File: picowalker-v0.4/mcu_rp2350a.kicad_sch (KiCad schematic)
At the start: 0 parts

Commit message: v0.4: schematic laid out first draft
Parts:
- added C1, C3, C7: 4.7u, Capacitor_SMD:C_0402_1005Metric, symbol Device:C
- added C10, C11, C12, C13, C14, C5, C6, C8, C9: 0.1u, Capacitor_SMD:C_0402_1005Metric, symbol Device:C
- added C2, C4: 15p, Capacitor_SMD:C_0201_0603Metric, symbol Device:C
- added L1: 3.3u, symbol picowalker:L_Polarised
- added R1: 33R, Resistor_SMD:R_0402_1005Metric, symbol Device:R
- added R2, R3, R4: 1k, Resistor_SMD:R_0402_1005Metric, symbol Device:R
- added R5, R6: 22R, Resistor_SMD:R_0402_1005Metric, symbol Device:R
- added SW1: ~{BOOT}, symbol picowalker:SW_SPST_Shield
- added SW2: RUN, symbol picowalker:SW_SPST_Shield
- added TP1: MCU_1V1, TestPoint:TestPoint_Pad_1.0x1.0mm, symbol Connector:TestPoint
- added U1: RP2350A-QFN60, symbol picowalker:RP2350A-QFN60
- added Y1: ABM8-272-T3, symbol Device:Crystal_GND24
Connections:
- new net: C4.1, R4.1, Y1.3
- new net: R6.1, U1.51 (USB_DM)
- new net: R5.1, U1.52 (USB_DP)
- new net: R2.2, SW2.1 (A)
- new net +1.1V: C1.1, C5.1, C6.1, C7.1, L1.1, TP1.1, U1.23 (DVDD), U1.39 (DVDD), U1.50 (VREG_FB), U1.6 (DVDD)
- new net +3.3V: C10.1, C11.1, C12.1, C13.1, C14.1, C8.1, C9.1, R1.1, U1.1 (IOVDD), U1.11 (IOVDD), U1.20 (IOVDD), U1.30 (IOVDD), U1.38 (IOVDD), U1.44 (ADC_AVDD), U1.45 (IOVDD), U1.49 (VREG_VIN), U1.53 (USB_OTP_VDD), U1.54 (QSPI_IOVDD)
- new net ACCEL_INT: U1.35 (GPIO23)
- new net DN: R6.2
- new net DP: R5.2
- new net GND: C1.2, C10.2, C11.2, C12.2, C13.2, C14.2, C2.2, C3.2, C4.2, C5.2, C6.2, C7.2, C8.2, C9.2, R2.1, SW1.1 (A), SW1.3 (SHIELD), SW2.3 (SHIELD), U1.47 (VREG_PGND), U1.61 (GND), Y1.2, Y1.4
- new net IRDA_SD: U1.19 (GPIO15)
- new net L: U1.28 (GPIO17)
- new net M: U1.27 (GPIO16)
- new net MISO: U1.32 (GPIO20)
- new net MOSI: U1.31 (GPIO19)
- new net PWR_EN: U1.9 (GPIO6)
- new net R: U1.40 (GPIO26_ADC0)
- new net RTC_CLK: U1.34 (GPIO22)
- new net RUN: SW2.2 (B), U1.26 (RUN)
- new net RX: U1.18 (GPIO14), U1.43 (GPIO29_ADC3)
- new net SCK: U1.12 (GPIO8), U1.29 (GPIO18), U1.56 (QSPI_SCLK)
- new net SCL: U1.3 (GPIO1)
- new net SD0: U1.16 (GPIO12), U1.57 (QSPI_SD0)
- new net SD1: U1.15 (GPIO11), U1.59 (QSPI_SD1)
- new net SD2: U1.14 (GPIO10), U1.58 (QSPI_SD2)
- new net SD3: U1.13 (GPIO9), U1.55 (QSPI_SD3)
- new net SDA: U1.2 (GPIO0)
- new net SOUND_PWM: U1.4 (GPIO2)
- new net SWCLK: U1.24 (SWCLK)
- new net SWDIO: U1.25 (SWDIO)
- new net TX: U1.17 (GPIO13), U1.42 (GPIO28_ADC2)
- new net VREG_AVDD: C3.1, R1.2, U1.46 (VREG_AVDD)
- new net VREG_LX: L1.2, U1.48 (VREG_LX)
- new net XIN: C2.1, U1.21 (XIN), Y1.1
- new net XOUT: R4.2, U1.22 (XOUT)
- new net ~{ACCEL_CS}: U1.33 (GPIO21)
- new net ~{BAT_INT}: U1.5 (GPIO3)
- new net ~{BOOT}: R3.1, SW1.2 (B)
- new net ~{CE}: U1.7 (GPIO4)
- new net ~{EEPROM_CS}: U1.36 (GPIO24)
- new net ~{FLASH_CS}: R3.2, U1.60 (QSPI_SS)
- new net ~{RST}: U1.10 (GPIO7)
- new net ~{SCREEN_CS}: U1.8 (GPIO5)
- no-connect marks 0 -> 2
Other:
- note added: "Ensure ground plane is >1.0 mm from surface"
- note added: "I2C0"
- note added: "PIO"
- note added: "SPI0"
- note added: "TODO: NEEDS CHECKING"

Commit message: v0.4: more rationalisation
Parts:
- added C37: 4.7u, Capacitor_SMD:C_0402_1005Metric, symbol Device:C
- R1: value 33R -> 47R
- TP1: now left out of the parts list
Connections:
- net +3.3V: now also C37.1
- net GND: now also C37.2
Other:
- note added: ""33R and 4.7u is adequate" -3 dB cutoff (1/2piRC) for 33R is 1026 Hz. 47R is 720 Hz."
- note removed: "TODO: NEEDS CHECKING"
- moved on the sheet: C1, C3, L1, R1, TP1

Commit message: v0.4: first rough placement of PCB
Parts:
- C1, C37: footprint Capacitor_SMD:C_0402_1005Metric -> picowalker:C_0402_1005Metric_Smaller
- L1: footprint (none) -> picowalker:L_0805_2016Metric
- SW1, SW2: footprint (none) -> picowalker:435151014824
- U1: footprint (none) -> Package_DFN_QFN:QFN-60-1EP_7x7mm_P0.4mm_EP3.4x3.4mm_ThermalVias
- Y1: footprint (none) -> picowalker:ABM8272T3
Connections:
- net DN renamed USB.DN
- net DP renamed USB.DP
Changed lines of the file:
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@@
 		)
 	)
-	(label "DP"
+	(label "USB.DP"
 		(at 208.28 44.45 0)
 		(effects
@@
 		)
 	)
-	(label "DN"
+	(label "USB.DN"
 		(at 208.28 46.99 0)
 		(effects
@@
 			)
 		)
-		(property "Footprint" "Capacitor_SMD:C_0402_1005Metric"
+		(property "Footprint" "picowalker:C_0402_1005Metric_Smaller"
 			(at 26.9748 39.37 0)
 			(effects
@@
 			)
 		)
-		(property "Footprint" ""
+		(property "Footprint" "Package_DFN_QFN:QFN-60-1EP_7x7mm_P0.4mm_EP3.4x3.4mm_ThermalVias"
 			(at 151.13 67.31 0)
 			(effects
@@
 			)
 		)
-		(property "Footprint" ""
+		(property "Footprint" "picowalker:L_0805_2016Metric"
 			(at 43.18 69.85 0)
 			(effects
@@
 			)
 		)
-		(property "Footprint" "Capacitor_SMD:C_0402_1005Metric"
+		(property "Footprint" "picowalker:C_0402_1005Metric_Smaller"
 			(at 53.0352 77.47 0)
 			(effects
@@
 			)
 		)
-		(property "Footprint" ""
+		(property "Footprint" "picowalker:ABM8272T3"
 			(at 38.1 168.91 0)
 			(effects
@@
 			)
 		)
-		(property "Footprint" ""
+		(property "Footprint" "picowalker:435151014824"
 			(at 44.45 130.81 0)
 			(effects
@@
 			)
 		)
-		(property "Footprint" ""
+		(property "Footprint" "picowalker:435151014824"
 			(at 31.75 106.68 0)
 			(effects

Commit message: v0.4: good start on routing
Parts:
- removed TP1: MCU_1V1, TestPoint:TestPoint_Pad_1.0x1.0mm, symbol Connector:TestPoint
- added R23, R24: 5.1k, Resistor_SMD:R_0402_1005Metric, symbol Device:R
- added TP6: GP16, picowalker:TestPoint_Pad_D1.0mm_Nosilk, symbol Connector:TestPoint
- added TP7: GP17, picowalker:TestPoint_Pad_D1.0mm_Nosilk, symbol Connector:TestPoint
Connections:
- net PWR_EN is gone; now on net ~{SCREEN_CS}: U1.9 (GPIO6)
- net +3.3V: now also R23.1, R24.1
- net IRDA_SD: now also U1.17 (GPIO13); no longer U1.19 (GPIO15)
- net ~{SCREEN_CS}: no longer U1.8 (GPIO5)
- net BUTTONS.L: now reaches U1.37 (GPIO25)
- net BUTTONS.R: now reaches U1.41 (GPIO27_ADC1)
- net L renamed GP17
- net GP17: now also TP7.1
- net M renamed GP16
- net GP16: now also TP6.1
- net MISO renamed SPI.MISO
- net MOSI renamed SPI.MOSI
- net R renamed BUTTONS.M
- net RX renamed DBG_UART.RX
- net DBG_UART.RX: no longer U1.18 (GPIO14)
- removed net SCK: U1.12 (GPIO8), U1.29 (GPIO18), U1.56 (QSPI_SCLK)
- net SCL renamed I2C.SCL
- net I2C.SCL: now also R24.2
- net SD0 renamed FLASH_QSPI.SD0
- net FLASH_QSPI.SD0: no longer U1.16 (GPIO12)
- net SD1 renamed FLASH_QSPI.SD1
- net FLASH_QSPI.SD1: no longer U1.15 (GPIO11)
- net SD2 renamed FLASH_QSPI.SD2
- net FLASH_QSPI.SD2: no longer U1.14 (GPIO10)
- net SD3 renamed FLASH_QSPI.SD3
- net FLASH_QSPI.SD3: no longer U1.13 (GPIO9)
- net SDA renamed I2C.SDA
- net I2C.SDA: now also R23.2
- net SWCLK renamed SWD.SWCLK
- net SWDIO renamed SWD.SWDIO
- net TX renamed DBG_UART.TX
- net DBG_UART.TX: no longer U1.17 (GPIO13)
- net ~{RST} renamed SCREEN_DATA.SCK
- new net FLASH_QSPI.SCK: U1.56 (QSPI_SCLK)
- new net IRDA.RX: U1.18 (GPIO14)
- new net IRDA.TX: U1.19 (GPIO15)
- new net SCREEN_AUX.PWR_EN: U1.8 (GPIO5)
- new net SCREEN_AUX.~{RST}: U1.16 (GPIO12)
- new net SCREEN_DATA.SD0: U1.15 (GPIO11)
- new net SCREEN_DATA.SD1: U1.14 (GPIO10)
- new net SCREEN_DATA.SD2: U1.13 (GPIO9)
- new net SCREEN_DATA.SD3: U1.12 (GPIO8)
- new net SPI.SCK: U1.29 (GPIO18)
- no-connect marks 2 -> 0

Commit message: v0.4: drc mostly done, need to fiddle with TH1
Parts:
- U1: footprint Package_DFN_QFN:QFN-60-1EP_7x7mm_P0.4mm_EP3.4x3.4mm_ThermalVias -> picowalker:QFN-60-1EP_7x7mm_P0.4mm_EP3.4x3.4mm_ThermalVias
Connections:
- net GND: now also SW2.1 (A); no longer R2.1
- net RUN: now also R2.2; no longer SW2.2 (B)
- new net SW_RUN_P: R2.1, SW2.2 (B)
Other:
- note added: "4.7u specifically on pin 23"
- moved on the sheet: R2, SW2
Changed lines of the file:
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@@
 		)
 	)
+	(text "4.7u specifically on pin 23"
+		(exclude_from_sim no)
+		(at 104.14 190.5 0)
+		(effects
+			(font
+				(size 1.27 1.27)
+			)
+		)
+	)
 	(text "I2C0"
 		(exclude_from_sim no)
@@
 	(wire
 		(pts
-			(xy 50.8 130.81) (xy 58.42 130.81)
+			(xy 36.83 130.81) (xy 50.8 130.81)
 		)
 		(stroke
@@
 	(wire
 		(pts
+			(xy 21.59 130.81) (xy 24.13 130.81)
+		)
+		(stroke
+			(width 0)
+			(type default)
+		)
+	)
+	(wire
+		(pts
 			(xy 193.04 74.93) (xy 223.52 74.93)
 		)
@@
 		)
 	)
-	(wire
-		(pts
-			(xy 34.29 130.81) (xy 38.1 130.81)
-		)
-		(stroke
-			(width 0)
-			(type default)
-		)
-	)
 	(bus
 		(pts
@@
 	(wire
 		(pts
-			(xy 21.59 130.81) (xy 26.67 130.81)
-		)
-		(stroke
-			(width 0)
-			(type default)
-		)
-	)
-	(wire
-		(pts
 			(xy 27.94 41.91) (xy 27.94 45.72)
 		)
@@
 	(wire
 		(pts
+			(xy 58.42 130.81) (xy 67.31 130.81)
+		)
+		(stroke
+			(width 0)
+			(type default)
+		)
+	)
+	(wire
+		(pts
 			(xy 38.1 106.68) (xy 46.99 106.68)
 		)
@@
 	(wire
 		(pts
-			(xy 44.45 135.89) (xy 21.59 135.89)
+			(xy 30.48 135.89) (xy 21.59 135.89)
 		)
 		(stroke
@@
 	)
 	(label "RUN"
-		(at 58.42 130.81 180)
+		(at 67.31 130.81 180)
 		(effects
 			(font
@@
 		)
 	)
+	(label "SW_RUN_P"
+		(at 38.1 130.81 0)
+		(effects
+			(font
+				(size 1.27 1.27)
+			)
+			(justify left bottom)
+		)
+	)
 	(label "VREG_PGND"
 		(at 114.3 59.69 0)
@@
 			)
 		)
-		(property "Footprint" "Package_DFN_QFN:QFN-60-1EP_7x7mm_P0.4mm_EP3.4x3.4mm_ThermalVias"
+		(property "Footprint" "picowalker:QFN-60-1EP_7x7mm_P0.4mm_EP3.4x3.4mm_ThermalVias"
 			(at 151.13 67.31 0)
 			(effects
@@
 	(symbol
 		(lib_id "picowalker:SW_SPST_Shield")
-		(at 44.45 130.81 0)
+		(at 30.48 130.81 0)
 		(unit 1)
 		(exclude_from_sim no)
@@
 		(fields_autoplaced yes)
 		(property "Reference" "SW2"
-			(at 44.45 123.19 0)
+			(at 30.48 123.19 0)
 			(effects
 				(font
@@
 		)
 		(property "Value" "RUN"
-			(at 44.45 125.73 0)
+			(at 30.48 125.73 0)
 			(effects
 				(font
@@
 		)
 		(property "Footprint" "picowalker:435151014824"
-			(at 44.45 130.81 0)
+			(at 30.48 130.81 0)
 			(effects
 				(font
@@
 		)
 		(property "Datasheet" "~"
-			(at 44.45 130.81 0)
+			(at 30.48 130.81 0)
 			(effects
 				(font
@@
 		)
 		(property "Description" "Single Pole Single Throw (SPST) switch"
-			(at 44.45 130.81 0)
+			(at 30.48 130.81 0)
 			(effects
 				(font
@@
 	(symbol
 		(lib_id "Device:R")
-		(at 30.48 130.81 90)
+		(at 54.61 130.81 90)
 		(unit 1)
 		(exclude_from_sim no)
@@
 		(fields_autoplaced yes)
 		(property "Reference" "R2"
-			(at 30.48 124.46 90)
+			(at 54.61 124.46 90)
 			(effects
 				(font
@@
 		)
 		(property "Value" "1k"
-			(at 30.48 127 90)
+			(at 54.61 127 90)
 			(effects
 				(font
@@
 		)
 		(property "Footprint" "Resistor_SMD:R_0402_1005Metric"
-			(at 30.48 132.588 90)
+			(at 54.61 132.588 90)
 			(effects
 				(font
@@
 		)
 		(property "Datasheet" "~"
-			(at 30.48 130.81 0)
+			(at 54.61 130.81 0)
 			(effects
 				(font
@@
 		)
 		(property "Description" "Resistor"
-			(at 30.48 130.81 0)
+			(at 54.61 130.81 0)
 			(effects
 				(font

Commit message: v0.4: idk, minimal changes
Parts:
- TP6, TP7: now left out of the parts list
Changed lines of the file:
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@@
 		(unit 1)
 		(exclude_from_sim no)
-		(in_bom yes)
+		(in_bom no)
 		(on_board yes)
 		(dnp no)
@@
 		(unit 1)
 		(exclude_from_sim no)
-		(in_bom yes)
-		(on_board yes)
-		(dnp no)
+		(in_bom no)
+		(on_board yes)
+		(dnp no)

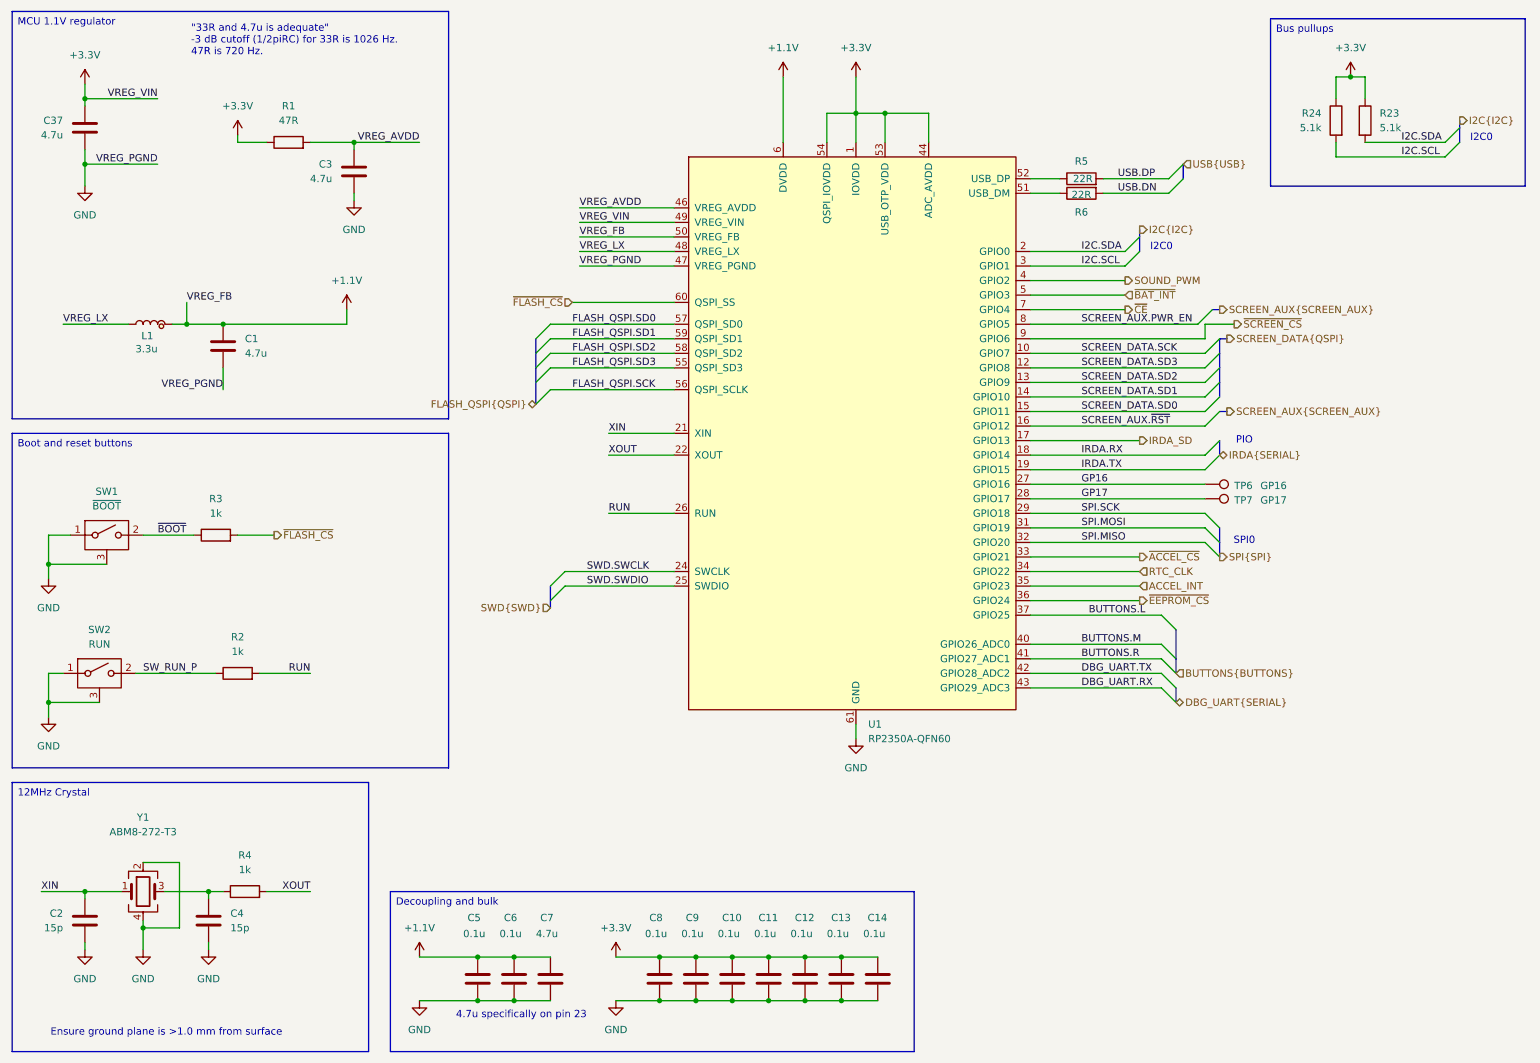
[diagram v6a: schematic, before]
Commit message: v0.4: add test points for touch pad
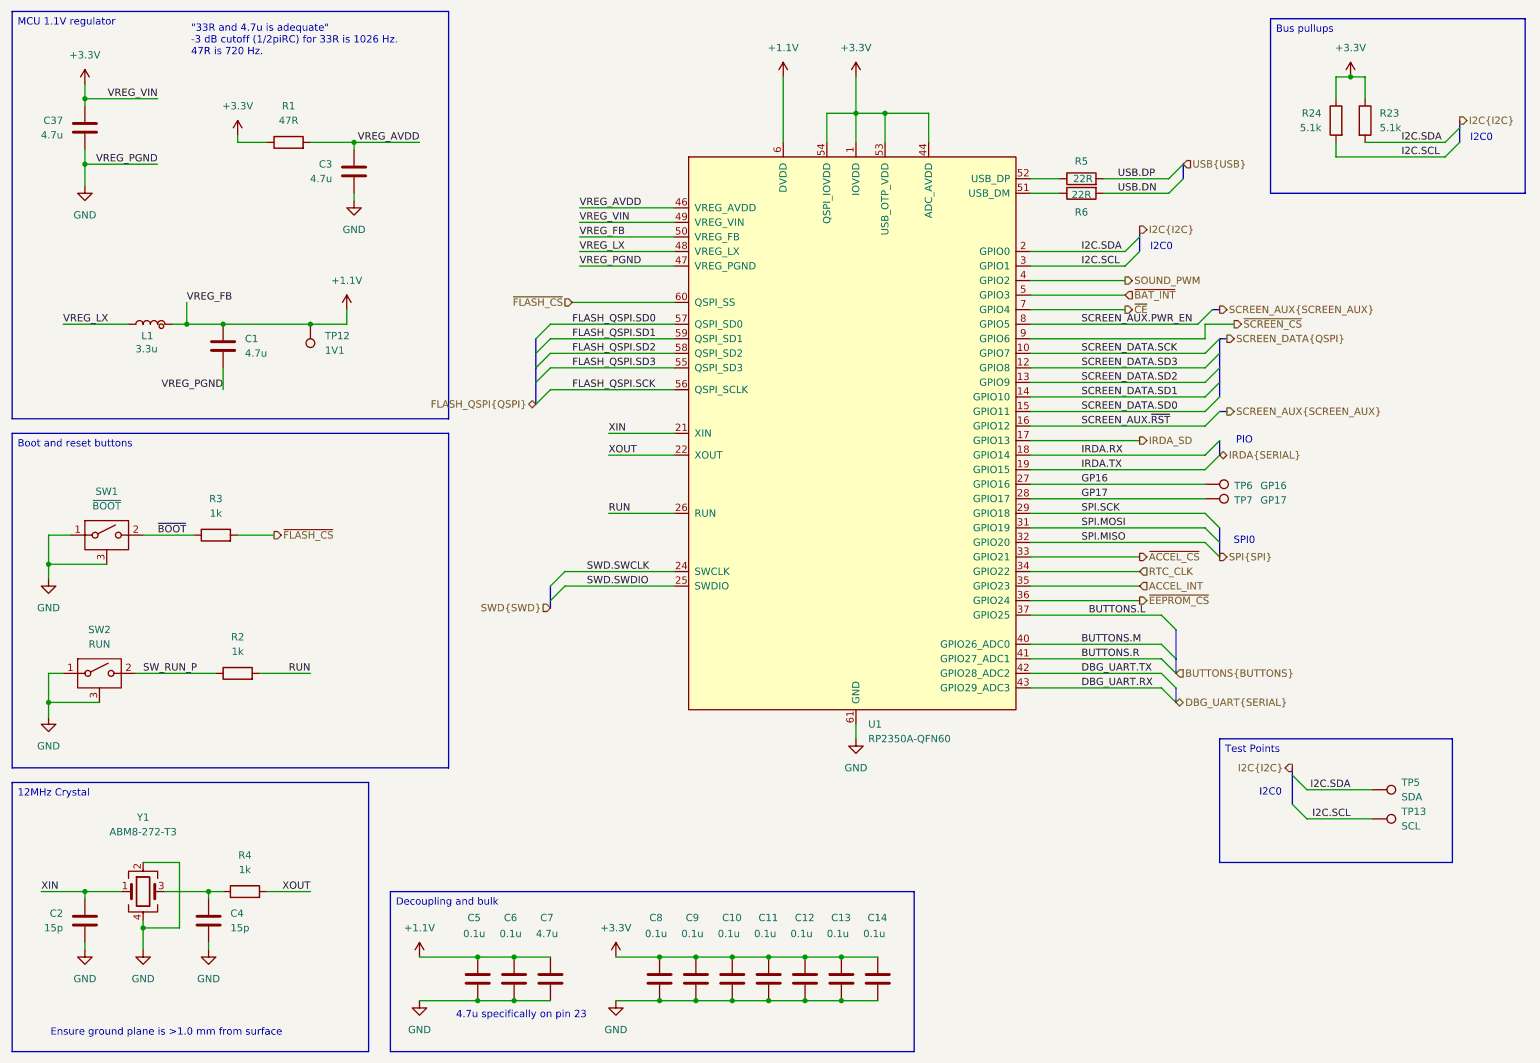
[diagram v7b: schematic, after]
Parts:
- added TP12: 1V1, picowalker:TestPoint_Pad_D1.0mm_Nosilk, symbol Connector:TestPoint
- added TP13: SCL, picowalker:TestPoint_Pad_D1.0mm_Nosilk, symbol Connector:TestPoint
- added TP5: SDA, picowalker:TestPoint_Pad_D1.0mm_Nosilk, symbol Connector:TestPoint
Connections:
- net +1.1V: now also TP12.1
- net I2C.SCL: now also TP13.1
- net I2C.SDA: now also TP5.1

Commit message: v0.4: change xtal caps to 0402
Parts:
- C2, C4: footprint Capacitor_SMD:C_0201_0603Metric -> Capacitor_SMD:C_0402_1005Metric
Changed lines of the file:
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@@
 			)
 		)
-		(property "Footprint" "Capacitor_SMD:C_0201_0603Metric"
+		(property "Footprint" "Capacitor_SMD:C_0402_1005Metric"
 			(at 26.9748 177.8 0)
 			(effects
@@
 			)
 		)
-		(property "Footprint" "Capacitor_SMD:C_0201_0603Metric"
+		(property "Footprint" "Capacitor_SMD:C_0402_1005Metric"
 			(at 50.4952 177.8 0)
 			(effects
